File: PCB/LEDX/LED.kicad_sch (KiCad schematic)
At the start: 26 parts, among them J2 Conn_01x03, J3 TC2030-USB-NL-DS, P1 Square, P2 Square, P3 Square, P4 Square, U1 ICS43434_MEMS_Mic, U2 ESP32-S3-MINI-1, U5 MD8942

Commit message: PCB Update
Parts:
- C4, C6: LCSC Part # C194427 -> (none); MPN (none) -> C194427
- C7: LCSC Part # C1691 -> (none); MPN (none) -> C1691
- D1: LCSC Part # C5349953 -> (none); MPN (none) -> C5349953
- D2: LCSC Part # C5137770 -> (none); MPN (none) -> C5137770
- J2: LCSC Part # C2765056 -> (none); MPN (none) -> C2765056
- U1: LCSC Part # C5656610 -> (none); MPN (none) -> C5656610
- U2: LCSC Part # C3013941 -> (none); MPN (none) -> C3013941
- U5: LCSC Part # C2684786 -> (none); MPN (none) -> C2684786
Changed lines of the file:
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@@
 			)
 		)
-		(property "LCSC Part #" "C1691"
+		(property "MPN" "C1691"
 			(at 254.635 41.275 0)
 			(effects
@@
 			)
 		)
-		(property "LCSC Part #" "C2684786"
+		(property "MPN" "C2684786"
 			(at 233.68 72.39 0)
 			(effects
@@
 			)
 		)
-		(property "LCSC Part #" "C194427"
+		(property "MPN" "C194427"
 			(at 254.635 39.37 0)
 			(effects
@@
 			)
 		)
-		(property "LCSC Part #" "C5349953"
+		(property "MPN" "C5349953"
 			(at 158.115 78.74 0)
 			(effects
@@
 			)
 		)
-		(property "LCSC Part #" "C194427"
+		(property "MPN" "C194427"
 			(at 150.495 66.675 0)
 			(effects
@@
 			)
 		)
-		(property "LCSC Part #" "C5656610"
+		(property "MPN" "C5656610"
 			(at 196.215 75.438 0)
 			(effects
@@
 			)
 		)
-		(property "LCSC Part #" "C5137770"
+		(property "MPN" "C5137770"
 			(at 181.61 100.965 0)
 			(effects
@@
 			)
 		)
-		(property "LCSC Part #" "C3013941"
+		(property "MPN" "C3013941"
 			(at 109.22 111.76 0)
 			(effects
@@
 			)
 		)
-		(property "LCSC Part #" "C2765056"
+		(property "MPN" "C2765056"
 			(at 201.295 97.155 0)
 			(effects

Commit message: Latest layout
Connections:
- net D-: now also J3.2 (NC), J3.6 (NC)
- net DC: no longer J3.2 (VBUS)
- net GND: no longer J3.6 (GND)
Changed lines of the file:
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@@
 			)
 		)
-		(property "Datasheet" " ~"
+		(property "Datasheet" "~"
 			(at 237.49 80.645 0)
 			(effects

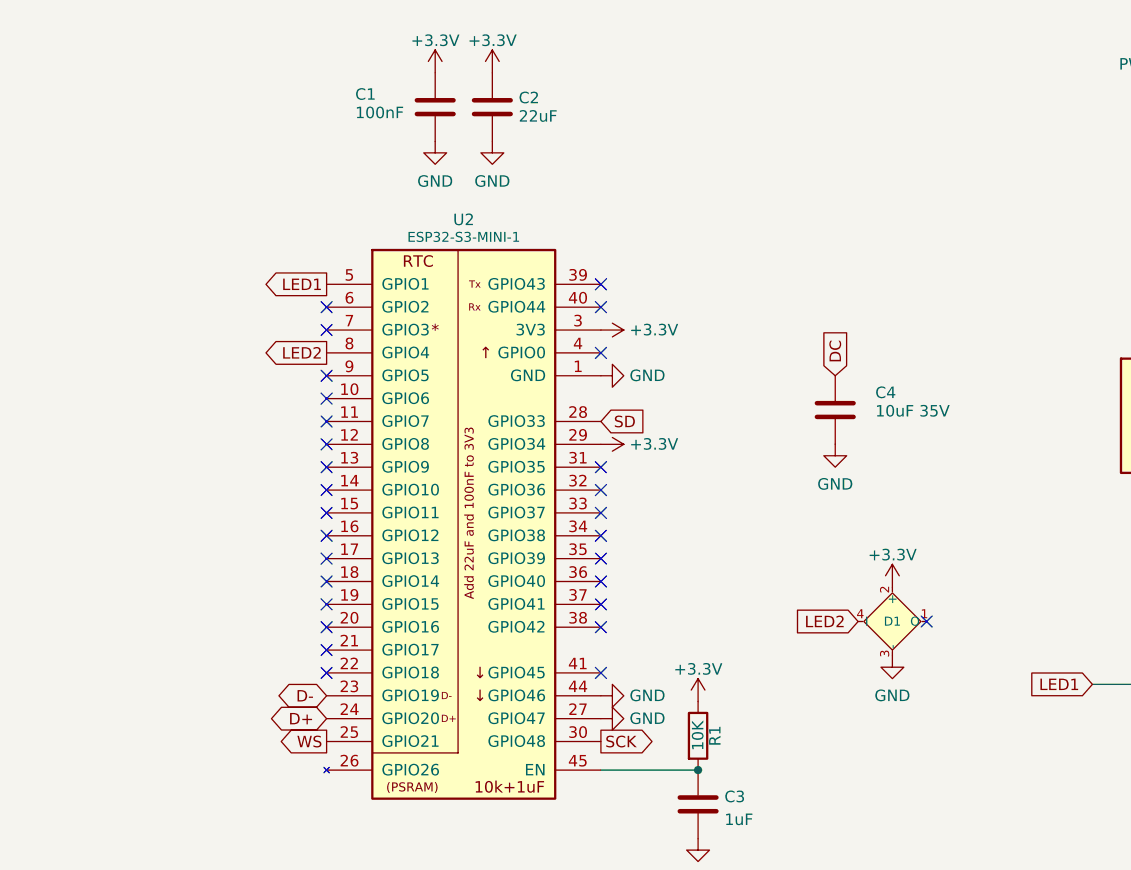
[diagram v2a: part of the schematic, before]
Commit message: More caps
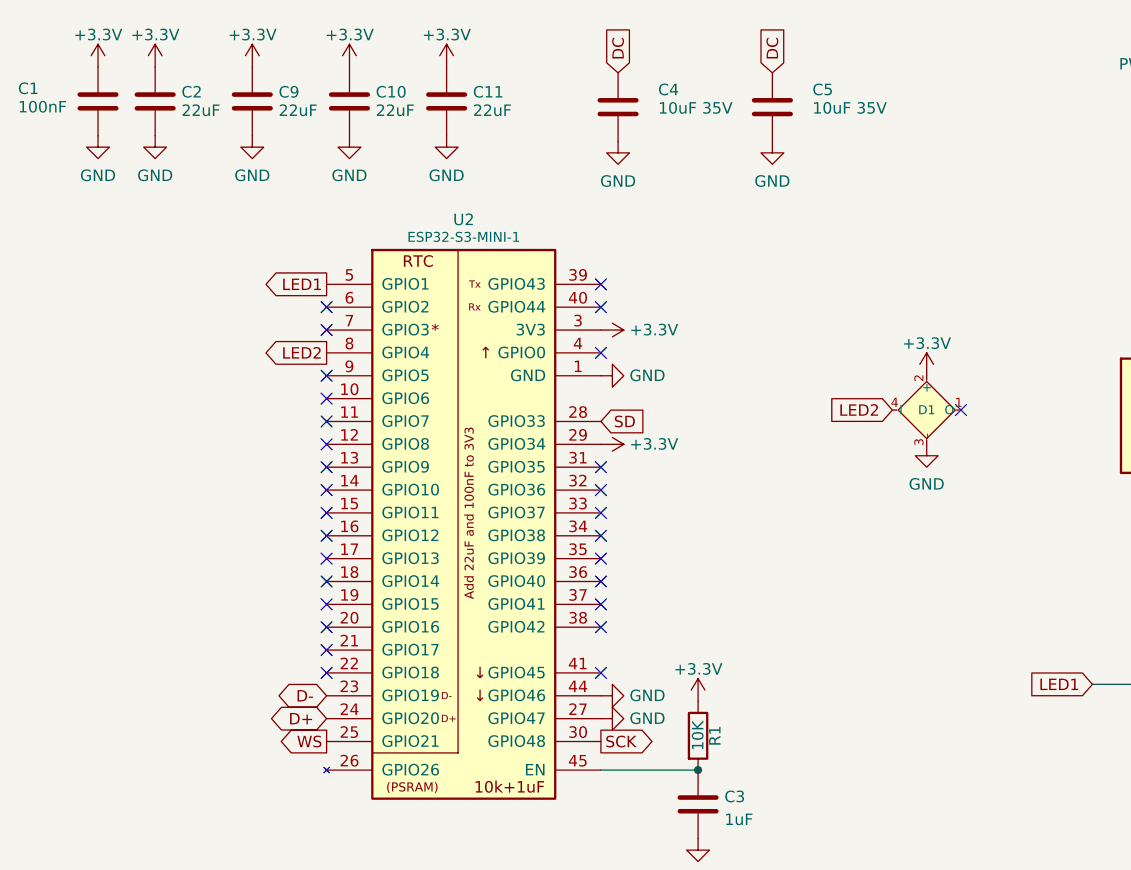
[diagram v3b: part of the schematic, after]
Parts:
- added C10, C11, C9: 22uF, RevK:C_0402, symbol Device:C
- added C5: 10uF 35V, RevK:C_0603, symbol Device:C
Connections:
- net +3.3V: now also C10.1, C11.1, C9.1
- net DC: now also C5.1
- net GND: now also C10.2, C11.2, C5.2, C9.2
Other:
- moved on the sheet: C1, C2, C4, D1

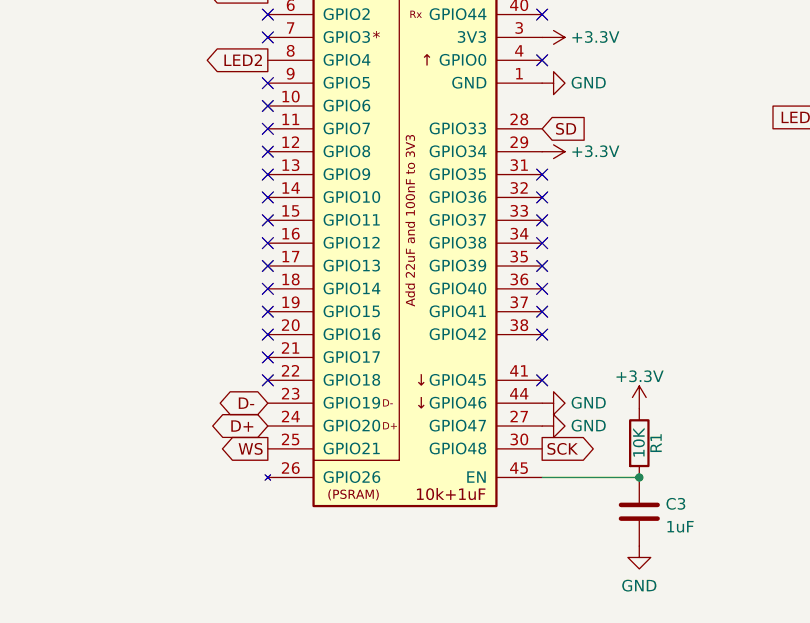
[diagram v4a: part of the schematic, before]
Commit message: Changed GPIO
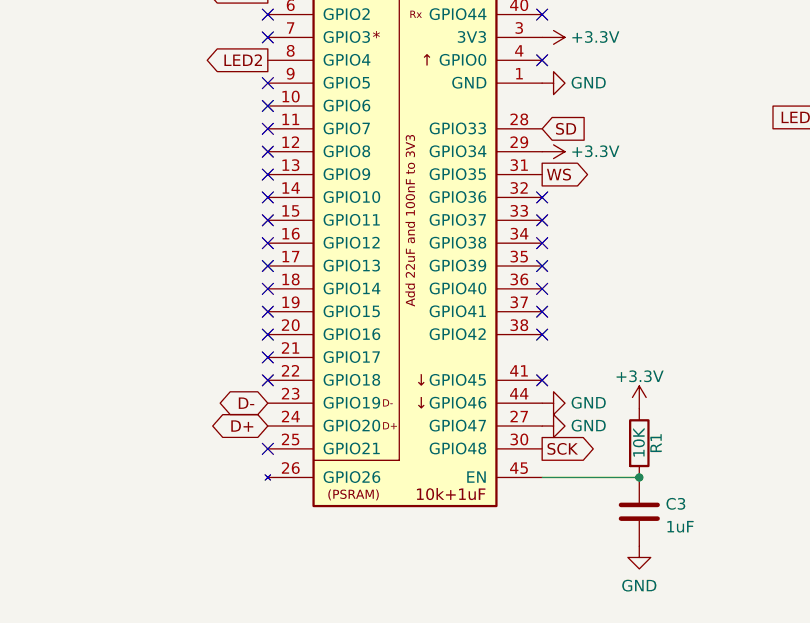
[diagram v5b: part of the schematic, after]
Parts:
- U1: footprint RevK:ICS43434_MEMS_Mic -> RevK:ICS43434_MEMS_Mic_Open
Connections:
- net WS: now also U2.31 (GPIO35); no longer U2.25 (GPIO21)
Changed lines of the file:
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@@
 	)
 	(no_connect
-		(at 124.46 73.025)
+		(at 93.98 103.505)
 	)
 	(no_connect
@@
 	(global_label "WS"
 		(shape output)
-		(at 93.98 103.505 180)
-		(fields_autoplaced yes)
-		(effects
-			(font
-				(size 1.27 1.27)
-			)
-			(justify right)
-		)
-		(property "Intersheetrefs" "${INTERSHEET_REFS}"
-			(at 88.9881 103.505 0)
-			(effects
-				(font
-					(size 1.27 1.27)
-				)
-				(justify right)
+		(at 124.46 73.025 0)
+		(fields_autoplaced yes)
+		(effects
+			(font
+				(size 1.27 1.27)
+			)
+			(justify left)
+		)
+		(property "Intersheetrefs" "${INTERSHEET_REFS}"
+			(at 129.4519 73.025 0)
+			(effects
+				(font
+					(size 1.27 1.27)
+				)
+				(justify left)
 				(hide yes)
 			)
@@
 			)
 		)
-		(property "Footprint" "RevK:ICS43434_MEMS_Mic"
+		(property "Footprint" "RevK:ICS43434_MEMS_Mic_Open"
 			(at 189.611 48.26 0)
 			(effects

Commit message: tidy
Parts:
- U1: footprint RevK:ICS43434_MEMS_Mic_Open -> RevK:ICS43434_MEMS_Mic
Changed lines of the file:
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@@
 			)
 		)
-		(property "Footprint" "RevK:ICS43434_MEMS_Mic_Open"
+		(property "Footprint" "RevK:ICS43434_MEMS_Mic"
 			(at 189.611 48.26 0)
 			(effects

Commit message: Updated (thicker case)
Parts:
- J2: footprint RevK:WAGO-2060-453-998-404 -> RevK:WAGO-2060-453-998-404-O
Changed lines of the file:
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@@
 			)
 		)
-		(property "Footprint" "RevK:WAGO-2060-453-998-404"
+		(property "Footprint" "RevK:WAGO-2060-453-998-404-O"
 			(at 201.295 97.155 0)
 			(effects

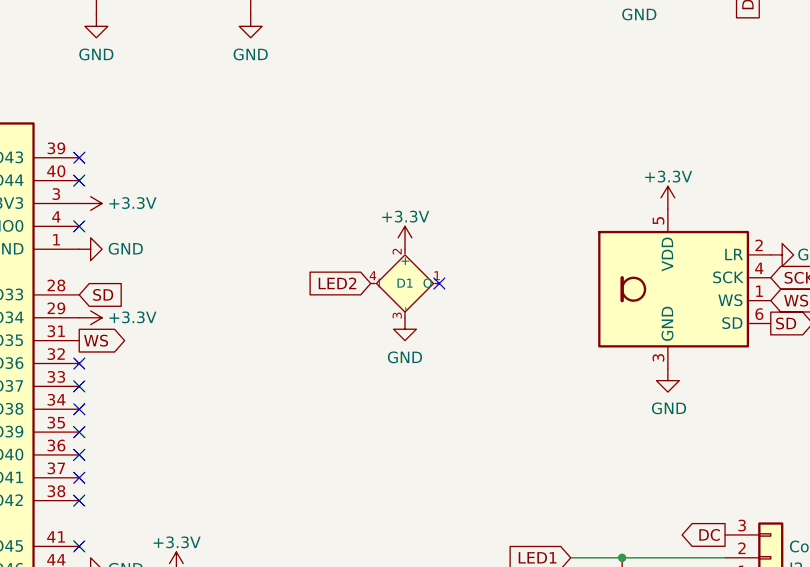
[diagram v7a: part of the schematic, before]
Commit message: New LEDs
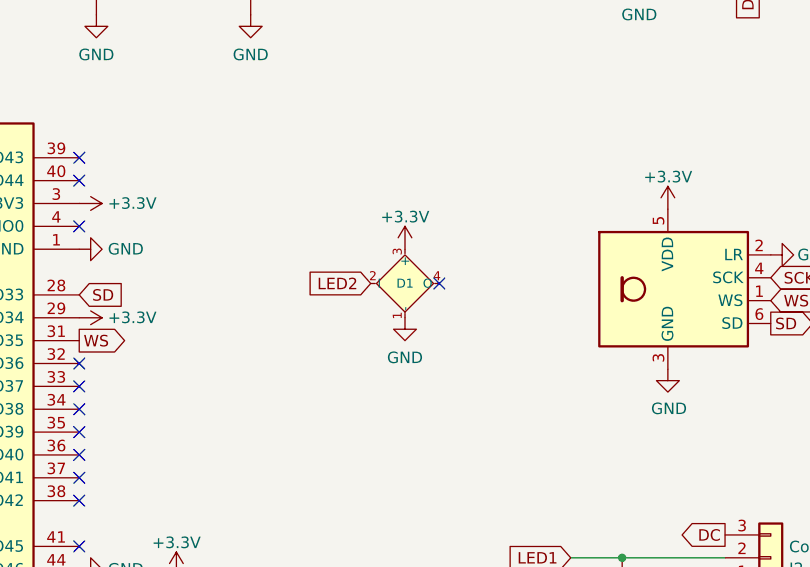
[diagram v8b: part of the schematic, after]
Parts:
- D1: footprint RevK:SMD1010 -> RevK:SMD1615; symbol RevK:WS2812B-1mm -> RevK:WS2812B-1.5mm; MPN C5349953 -> C5349954
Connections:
- net +3.3V: now also D1.3 (+); no longer D1.2 (+)
- net GND: now also D1.1 (-); no longer D1.3 (-)
- net LED2: now also D1.2 (I); no longer D1.4 (I)
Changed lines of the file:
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@@
 	)
 	(symbol
-		(lib_id "RevK:WS2812B-1mm")
+		(lib_id "RevK:WS2812B-1.5mm")
 		(at 160.655 66.675 0)
-		(mirror x)
 		(unit 1)
 		(exclude_from_sim no)
@@
 		)
 		(property "Value" "XL-1010RGBC-WS2812B"
-			(at 161.925 60.96 0)
+			(at 161.925 72.39 0)
 			(effects
 				(font
@@
 			)
 		)
-		(property "Footprint" "RevK:SMD1010"
+		(property "Footprint" "RevK:SMD1615"
 			(at 161.925 59.055 0)
 			(effects
@@
 			)
 		)
-		(property "Datasheet" "https://datasheet.lcsc.com/lcsc/2301111010_XINGLIGHT-XL-1010RGBC-WS2812B_C5349953.pdf"
+		(property "Datasheet" "https://www.lcsc.com/datasheet/C5349954.pdf"
 			(at 161.925 57.15 0)
 			(effects
@@
 			)
 		)
-		(property "MPN" "C5349953"
+		(property "MPN" "C5349954"
 			(at 161.925 55.245 0)
 			(effects
